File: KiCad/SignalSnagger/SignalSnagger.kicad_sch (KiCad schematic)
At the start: 52 parts, among them Q2 MMBT2222A, Q3 MMBT2222A, SW1 Sense, T1 Transformer_1P_SS

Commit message: Schematic Update
Development
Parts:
- C?: value (none) -> 47nF
- C? (x2): value (none) -> 100nF
- C?: value (none) -> 10nF
- C?: value (none) -> 4.7uF
- C?: value (none) -> 390pF
- R?: value (none) -> 1k
- R?: value (none) -> ??
- R?: value (none) -> 4.99k
- R?: value (none) -> 10
- U? (x2): value (none) -> LT6231
- U?: value (none) -> SN74CBT3253
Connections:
- net at C?.1, C?.1, C?.1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: now also U?.5 (+)
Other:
- moved on the sheet: C?, R?, U?A, U?B

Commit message: Schematic Update
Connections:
- net +5V: now also C?.1, R?.1, U?.8 (V+)
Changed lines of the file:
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@@
+    (pin "1")
+  )
+  (symbol (lib_id "power:+5V") (at 218.44 92.71 0) (unit 1)
+    (in_bom yes) (on_board yes) (fields_autoplaced)
+    (property "Reference" "#PWR?" (id 0) (at 218.44 96.52 0)
+      (effects (font (size 1.27 1.27)) hide)
+    )
+    (property "Value" "+5V" (id 1) (at 218.44 89.1342 0))
+    (property "Footprint" "" (id 2) (at 218.44 92.71 0)
+      (effects (font (size 1.27 1.27)) hide)
+    )
+    (property "Datasheet" "" (id 3) (at 218.44 92.71 0)
+      (effects (font (size 1.27 1.27)) hide)
+    )
     (pin "1")
   )
@@
       (reference "#PWR?") (unit 1) (value "GND") (footprint "")
     )
+    (path "/e940abae-4b03-4d64-833d-2c2a8f4b7ce6"
+      (reference "#PWR?") (unit 1) (value "+5V") (footprint "")
+    )
     (path "/ee2b8b61-78d4-4be1-bcfa-07bf2321c210"

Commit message: Schematic Updates
Development
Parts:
- removed SW1: Sense, symbol Switch:SW_SPDT
- added SW101: (no value), symbol Switch:SW_SPDT_MSM
- gave numbers to parts that had none: 28
- renumbered AE1 to AE101, AE2 to AE102, C1 to C101, C2 to C102, C4 to C103, C3 to C104, C5 to C105, C6 to C106, C7 to C107, C8 to C110, Q2 to Q102, Q3 to Q103, R1 to R101, R2 to R102, R5 to R103, R6 to R104, R4 to R105, R7 to R106, R8 to R107, RV1 to RV101, T1 to T101
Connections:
- net at AE102.1 (Sense_A): now also SW101.1
- net at Q101.2 (E): now also SW101.2
- net at AE102.3 (Sense_B): now also SW101.3
- net CLK IN renamed QSD_CLK
- no-connect marks 2 -> 6
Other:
- added sheet Audio (audio.kicad_sch)
- added sheet Processor (processor.kicad_sch)

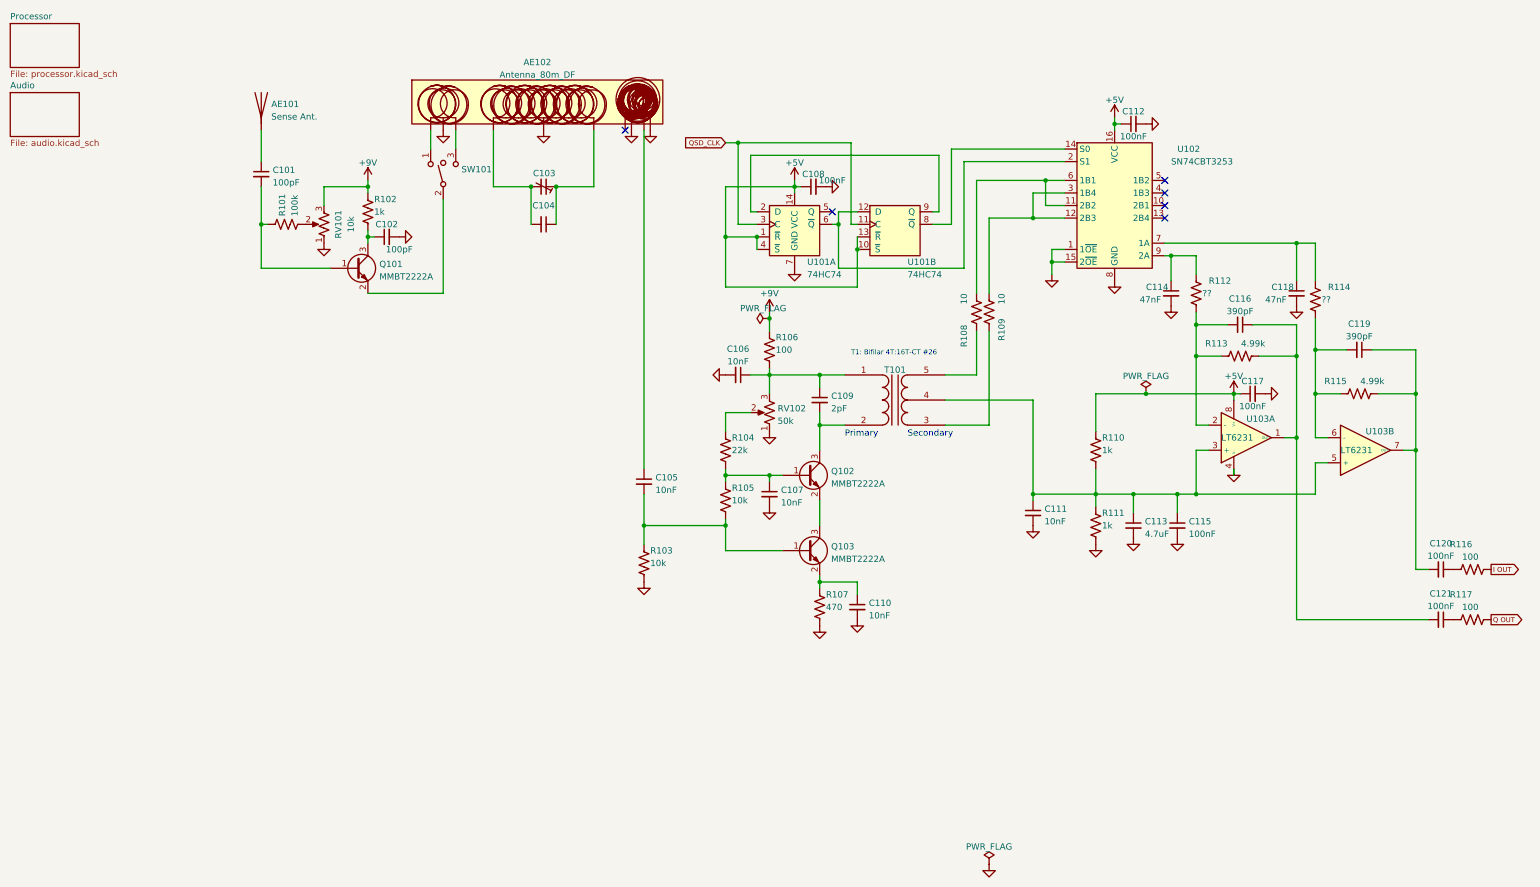
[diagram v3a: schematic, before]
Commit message: Schematic Update
DF Antenna Corrections
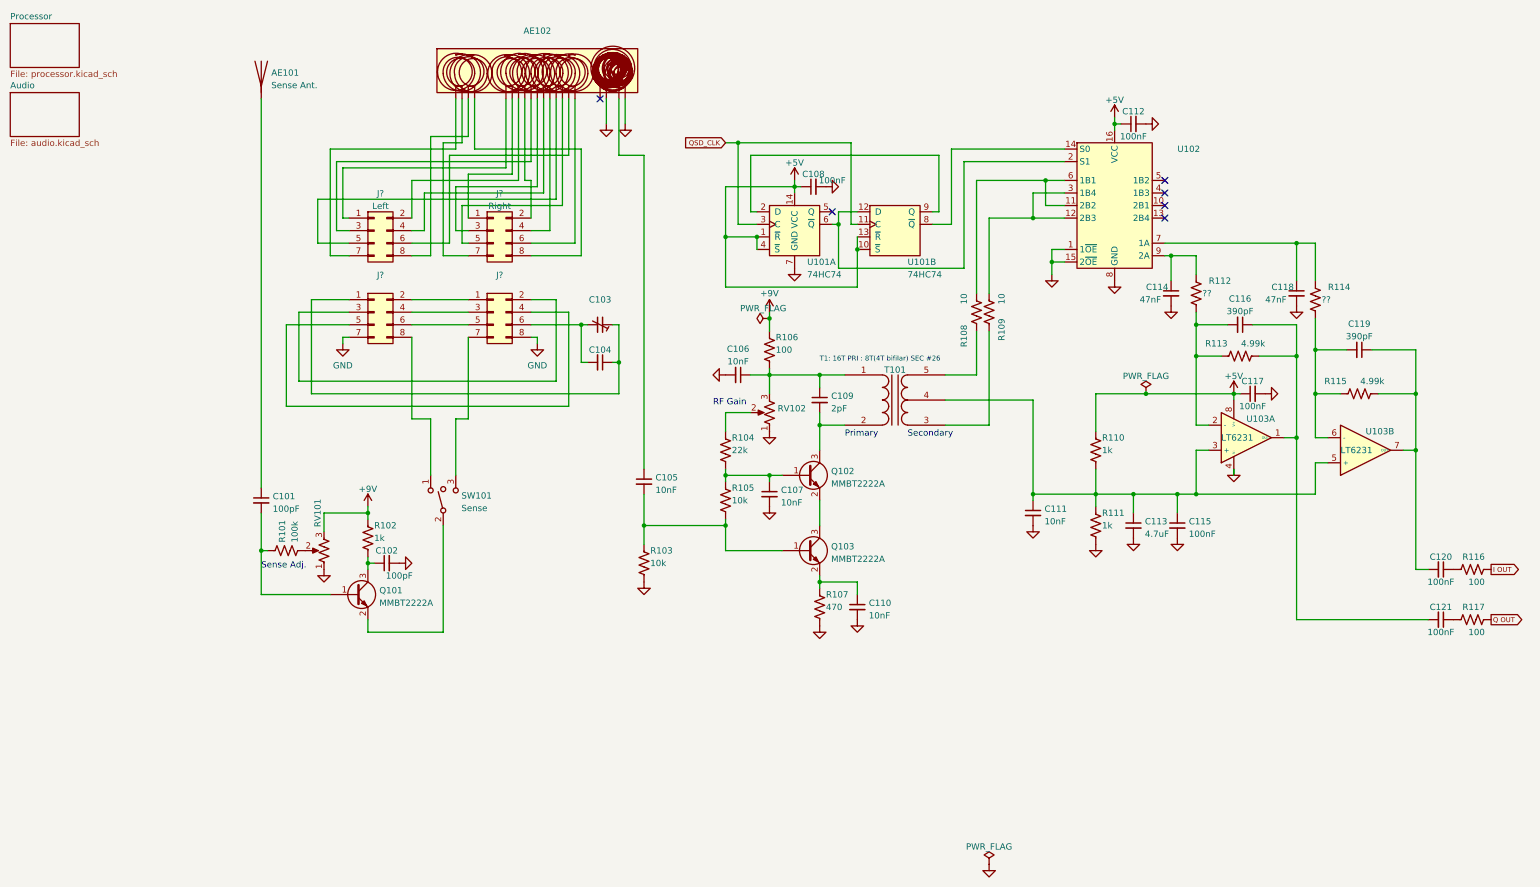
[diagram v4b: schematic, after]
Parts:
- added J? (x2): (no value), symbol Connector_Generic:Conn_02x04_Odd_Even
- added J?: Left, symbol Connector_Generic:Conn_02x04_Odd_Even
- added J?: Right, symbol Connector_Generic:Conn_02x04_Odd_Even
- AE102: value Antenna_80m_DF -> (none)
- C103: value C_Trim_Small -> (none); Link (none) -> https://www.jameco.com/z/CTC07RB-100-Jameco-ValuePro-Capaci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; Manufacturer PN (none) -> CTC07RB-100
- C104: value C_Small -> (none)
- RV101: value 10k -> (none)
- RV102: value 50k -> (none)
- SW101: value (none) -> Sense
- U102: value SN74CBT3253 -> (none)
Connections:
- net GND: now also AE102.18 (Pickup_A), AE102.20 (Shield_B), J?.7 (Pin_7), J?.8 (Pin_8); no longer AE102.10 (Shield_B), AE102.2 (Sense_CT), AE102.5 (Loop_CT), AE102.8 (Pickup_A)
- net at C103.1, C104.1: now also J?.1 (Pin_1); no longer AE102.6 (Loop_2)
- net at C103.2, C104.2: now also J?.6 (Pin_6); no longer AE102.4 (Loop_1)
- net at AE102.1 (SenseA_A): now also J?.7 (Pin_7); no longer SW101.1
- net at SW101.3: now also J?.7 (Pin_7); no longer AE102.3 (Sense_B)
- net at AE102.7 (Loop_2A): now also J?.2 (Pin_2)
- net at AE102.9 (Loop_3A): now also J?.3 (Pin_3); no longer C105.1
- new net: J?.1 (Pin_1), J?.2 (Pin_2)
- new net: J?.2 (Pin_2), J?.3 (Pin_3)
- new net: J?.3 (Pin_3), J?.4 (Pin_4)
- new net: J?.4 (Pin_4), J?.5 (Pin_5)
- new net: J?.5 (Pin_5), J?.6 (Pin_6)
- new net: AE102.5 (Loop_1A), J?.1 (Pin_1)
- new net: AE102.11 (Loop_4A), J?.4 (Pin_4)
- new net: AE102.13 (Loop_7A), J?.5 (Pin_5)
- new net: AE102.15 (Loop_8A), J?.6 (Pin_6)
- new net: AE102.3 (SenseB_A), J?.8 (Pin_8)
- new net: AE102.6 (Loop_1B), J?.1 (Pin_1)
- new net: AE102.8 (Loop_2B), J?.2 (Pin_2)
- new net: AE102.10 (Loop_3B), J?.3 (Pin_3)
- new net: AE102.12 (Loop_6B), J?.4 (Pin_4)
- new net: AE102.14 (Loop_7B), J?.5 (Pin_5)
- new net: AE102.16 (Loop_8B), J?.6 (Pin_6)
- new net: AE102.2 (SenseA-B), J?.7 (Pin_7)
- new net: AE102.4 (SenseB_B), J?.8 (Pin_8)
- new net: J?.8 (Pin_8), SW101.1
- new net: AE102.19 (Pickup_B), C105.1
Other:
- note added: "RF Gain"
- note added: "Sense Adj."
- note added: "T1: 16T PRI : 8T(4T bifilar) SEC #26"
- note removed: "T1: Bifilar 4T:16T-CT #26"
- moved on the sheet: AE101, AE102, C101, C102, C103, C104, Q101, R101, R102, RV101, SW101

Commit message: Ver 0.6
Schematic updates
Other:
- note added: "Ribbon Cable"
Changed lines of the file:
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@@
   (title_block
     (title "SignalSnagger")
-    (date "2023-11-04")
-    (rev "0.5")
+    (date "2023-11-05")
+    (rev "0.6")
   )
   (junction (at 190.5 113.03) (diameter 0) (color 0 0 0 0)
@@
     (effects (font (size 1.27 1.27)) (justify left bottom))
   )
+  (text "Ribbon Cable" (at 77.47 27.94 180)
+    (effects (font (size 1.27 1.27)) (justify right bottom))
+  )
   (text "Sense Adj." (at 21.59 128.27 0)

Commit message: Ver 0.6
Re-annotated and ERC'd
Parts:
- gave numbers to parts that had none: 4

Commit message: Ver 0.7
Schematic update
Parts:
- added J105, J106, J107: (no value), symbol Connector_Generic:Conn_01x01
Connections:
- net GND: now also J106.1 (Pin_1), J107.1 (Pin_1)
- net at AE102.19 (Pickup_B), C105.1: now also J105.1 (Pin_1)
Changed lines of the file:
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@@
     (title "SignalSnagger")
     (date "2023-11-05")
-    (rev "0.6")
+    (rev "0.7")
   )
   (junction (at 190.5 113.03) (diameter 0) (color 0 0 0 0)
@@
   (junction (at 255.27 92.71) (diameter 0) (color 0 0 0 0)
   )
+  (junction (at 101.6 52.07) (diameter 0) (color 0 0 0 0)
+  )
+  (junction (at 90.17 52.07) (diameter 0) (color 0 0 0 0)
+  )
   (junction (at 231.14 85.09) (diameter 0) (color 0 0 0 0)
   )
@@
   )
   (junction (at 231.14 101.6) (diameter 0) (color 0 0 0 0)
+  )
+  (junction (at 99.06 59.69) (diameter 0) (color 0 0 0 0)
   )
   (junction (at 200.66 92.71) (diameter 0) (color 0 0 0 0)
@@
     (stroke (width 0) (type default) (color 0 0 0 0))
   )
+  (wire (pts (xy 95.25 38.1) (xy 101.6 38.1))
+    (stroke (width 0) (type default) (color 0 0 0 0))
+  )
   (wire (pts (xy 35.56 64.77) (xy 39.37 64.77))
     (stroke (width 0) (type default) (color 0 0 0 0))
@@
     (stroke (width 0) (type default) (color 0 0 0 0))
   )
+  (wire (pts (xy 90.17 48.26) (xy 90.17 52.07))
+    (stroke (width 0) (type default) (color 0 0 0 0))
+  )
   (wire (pts (xy 124.46 87.63) (xy 124.46 88.9))
     (stroke (width 0) (type default) (color 0 0 0 0))
@@
     (stroke (width 0) (type default) (color 0 0 0 0))
   )
+  (wire (pts (xy 101.6 38.1) (xy 101.6 52.07))
+    (stroke (width 0) (type default) (color 0 0 0 0))
+  )
   (wire (pts (xy 73.66 49.53) (xy 73.66 33.02))
     (stroke (width 0) (type default) (color 0 0 0 0))
@@
     (stroke (width 0) (type default) (color 0 0 0 0))
   )
-  (wire (pts (xy 99.06 107.95) (xy 99.06 44.45))
+  (wire (pts (xy 99.06 107.95) (xy 99.06 59.69))
     (stroke (width 0) (type default) (color 0 0 0 0))
   )
@@
     (stroke (width 0) (type default) (color 0 0 0 0))
   )
+  (wire (pts (xy 91.44 48.26) (xy 90.17 48.26))
+    (stroke (width 0) (type default) (color 0 0 0 0))
+  )
   (wire (pts (xy 21.59 133.35) (xy 21.59 124.46))
     (stroke (width 0) (type default) (color 0 0 0 0))
@@
     (stroke (width 0) (type default) (color 0 0 0 0))
   )
+  (wire (pts (xy 99.06 59.69) (xy 99.06 44.45))
+    (stroke (width 0) (type default) (color 0 0 0 0))
+  )
   (wire (pts (xy 234.95 92.71) (xy 240.03 92.71))
     (stroke (width 0) (type default) (color 0 0 0 0))
@@
     (stroke (width 0) (type default) (color 0 0 0 0))
   )
-  (wire (pts (xy 91.44 33.02) (xy 91.44 38.1))
+  (wire (pts (xy 91.44 33.02) (xy 91.44 48.26))
     (stroke (width 0) (type default) (color 0 0 0 0))
   )
@@
     (pin "2")
   )
+  (symbol (lib_id "Connector_Generic:Conn_01x01") (at 104.14 59.69 0) (unit 1)
+    (in_bom yes) (on_board yes)
+    (property "Reference" "J105" (id 0) (at 106.172 58.8553 0)
+      (effects (font (size 1.27 1.27)) (justify left))
+    )
+    (property "Value" "" (id 1) (at 100.33 63.5 0)
+      (effects (font (size 1.27 1.27)) (justify left))
+    )
+    (property "Footprint" "" (id 2) (at 104.14 59.69 0)
+      (effects (font (size 1.27 1.27)) hide)
+    )
+    (property "Datasheet" "~" (id 3) (at 104.14 59.69 0)
+      (effects (font (size 1.27 1.27)) hide)
+    )
+    (pin "1")
+  )
   (symbol (lib_id "Amplifier_Operational:LT6231") (at 245.11 104.14 0) (mirror x) (unit 2)
     (in_bom yes) (on_board yes)
@@
     )
     (property "Datasheet" "" (id 3) (at 194.31 36.83 0)
-      (effects (font (size 1.27 1.27)) hide)
-    )
-    (pin "1")
-  )
-  (symbol (lib_id "power:GND") (at 95.25 38.1 0) (unit 1)
-    (in_bom yes) (on_board yes) (fields_autoplaced)
-    (property "Reference" "#PWR0107" (id 0) (at 95.25 44.45 0)
-      (effects (font (size 1.27 1.27)) hide)
-    )
-    (property "Value" "GND" (id 1) (at 95.6838 41.2749 90)
-      (effects (font (size 1.27 1.27)) (justify right) hide)
-    )
-    (property "Footprint" "" (id 2) (at 95.25 38.1 0)
-      (effects (font (size 1.27 1.27)) hide)
-    )
-    (property "Datasheet" "" (id 3) (at 95.25 38.1 0)
       (effects (font (size 1.27 1.27)) hide)
     )
@@
     (pin "2")
   )
+  (symbol (lib_id "Connector_Generic:Conn_01x01") (at 95.25 52.07 0) (unit 1)
+    (in_bom yes) (on_board yes)
+    (property "Reference" "J106" (id 0) (at 93.98 49.53 0)
+      (effects (font (size 1.27 1.27)) (justify left))
+    )
+    (property "Value" "" (id 1) (at 87.63 55.88 0)
+      (effects (font (size 1.27 1.27)) (justify left))
+    )
+    (property "Footprint" "" (id 2) (at 95.25 52.07 0)
+      (effects (font (size 1.27 1.27)) hide)
+    )
+    (property "Datasheet" "~" (id 3) (at 95.25 52.07 0)
+      (effects (font (size 1.27 1.27)) hide)
+    )
+    (pin "1")
+  )
   (symbol (lib_id "Device:R_US") (at 234.95 73.66 180) (unit 1)
     (in_bom yes) (on_board yes)
@@
     (pin "2")
   )
-  (symbol (lib_id "power:GND") (at 91.44 38.1 0) (unit 1)
-    (in_bom yes) (on_board yes) (fields_autoplaced)
-    (property "Reference" "#PWR0106" (id 0) (at 91.44 44.45 0)
-      (effects (font (size 1.27 1.27)) hide)
-    )
-    (property "Value" "GND" (id 1) (at 91.8738 41.2749 90)
+  (symbol (lib_id "power:GND") (at 90.17 52.07 0) (unit 1)
+    (in_bom yes) (on_board yes) (fields_autoplaced)
+    (property "Reference" "#PWR0106" (id 0) (at 90.17 58.42 0)
+      (effects (font (size 1.27 1.27)) hide)
+    )
+    (property "Value" "GND" (id 1) (at 90.6038 55.2449 90)
       (effects (font (size 1.27 1.27)) (justify right) hide)
     )
-    (property "Footprint" "" (id 2) (at 91.44 38.1 0)
-      (effects (font (size 1.27 1.27)) hide)
-    )
-    (property "Datasheet" "" (id 3) (at 91.44 38.1 0)
+    (property "Footprint" "" (id 2) (at 90.17 52.07 0)
+      (effects (font (size 1.27 1.27)) hide)
+    )
+    (property "Datasheet" "" (id 3) (at 90.17 52.07 0)
       (effects (font (size 1.27 1.27)) hide)
     )
@@
     (pin "1")
   )
+  (symbol (lib_id "Connector_Generic:Conn_01x01") (at 106.68 52.07 0) (unit 1)
+    (in_bom yes) (on_board yes)
+    (property "Reference" "J107" (id 0) (at 105.41 49.53 0)
+      (effects (font (size 1.27 1.27)) (justify left))
+    )
+    (property "Value" "" (id 1) (at 101.6 55.88 0)
+      (effects (font (size 1.27 1.27)) (justify left))
+    )
+    (property "Footprint" "" (id 2) (at 106.68 52.07 0)
+      (effects (font (size 1.27 1.27)) hide)
+    )
+    (property "Datasheet" "~" (id 3) (at 106.68 52.07 0)
+      (effects (font (size 1.27 1.27)) hide)
+    )
+    (pin "1")
+  )
   (symbol (lib_id "power:GND") (at 134.62 139.7 0) (mirror y) (unit 1)
     (in_bom yes) (on_board yes) (fields_autoplaced)
@@
     )
     (property "Datasheet" "" (id 3) (at 218.44 92.71 0)
+      (effects (font (size 1.27 1.27)) hide)
+    )
+    (pin "1")
+  )
+  (symbol (lib_id "power:GND") (at 101.6 52.07 0) (unit 1)
+    (in_bom yes) (on_board yes) (fields_autoplaced)
+    (property "Reference" "#PWR0107" (id 0) (at 101.6 58.42 0)
+      (effects (font (size 1.27 1.27)) hide)
+    )
+    (property "Value" "GND" (id 1) (at 102.0338 55.2449 90)
+      (effects (font (size 1.27 1.27)) (justify right) hide)
+    )
+    (property "Footprint" "" (id 2) (at 101.6 52.07 0)
+      (effects (font (size 1.27 1.27)) hide)
+    )
+    (property "Datasheet" "" (id 3) (at 101.6 52.07 0)
       (effects (font (size 1.27 1.27)) hide)
     )
@@
       (reference "#PWR0106") (unit 1) (value "GND") (footprint "")
     )
-    (path "/28d89845-7c3d-46a4-9779-eda7967c8483"
+    (path "/ec23a1d0-b47e-4390-94b0-18c2ba8c4381"
       (reference "#PWR0107") (unit 1) (value "GND") (footprint "")
     )
@@
       (reference "J104") (unit 1) (value "Right") (footprint "")
     )
+    (path "/1827fd48-a0ad-4504-ad60-021c20fdb5f0"
+      (reference "J105") (unit 1) (value "36-5005-ND") (footprint "")
+    )
+    (path "/8ba8ca84-fe11-4451-98ef-b0eb79cb42a9"
+      (reference "J106") (unit 1) (value "36-5006-ND") (footprint "")
+    )
+    (path "/e10dfb72-98a3-4565-ab0f-62e619d1350e"
+      (reference "J107") (unit 1) (value "36-5006-ND") (footprint "")
+    )
     (path "/b7e6c0d8-791a-469a-85d5-f8e886443224/87efc960-fc20-4947-aae8-fb6b9c89ea87"
